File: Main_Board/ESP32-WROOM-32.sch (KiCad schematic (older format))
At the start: 19 parts, among them J1 USB_B_Micro, Q1 mmbt2222, Q2 mmbt2222, U1 CP2104, U3 ESP32-WROOM-32

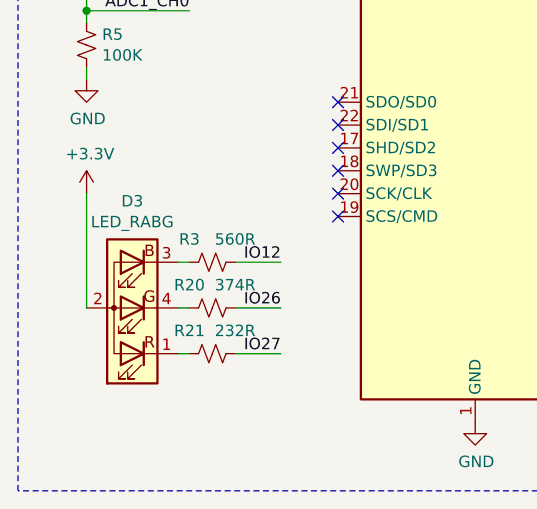
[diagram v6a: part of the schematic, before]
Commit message: New D3 footprint and model
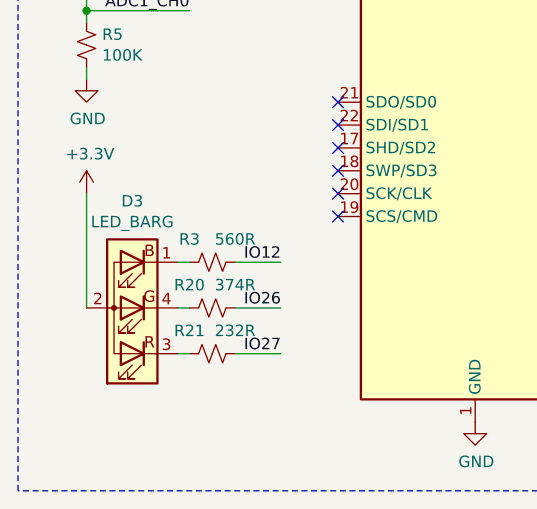
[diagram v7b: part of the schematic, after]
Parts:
- removed D3: LED_RABG, Main_Board:LED_QBLP655R_RGB, symbol Device:LED_RABG
- added D3: LED_BARG, Main_Board:LED-160-80180, symbol Device:LED_BARG
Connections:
- net +3V3: now also D3.2 (A)
- net at R3.2: now also D3.1 (BK)
- net at R20.2: now also D3.4 (GK)
- net at R21.2: now also D3.3 (RK)
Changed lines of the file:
@@
 	3400 3650 3650 3650
 NoConn ~ 3400 2450
+NoConn ~ 2200 2950
+NoConn ~ 2200 3050
 $Comp
-L Device:LED_RABG D3
-U 1 1 5FFE32BD
+L Device:LED_BARG D3
+U 1 1 60BEE694
 P 1300 3850
 F 0 "D3" H 1300 3383 50  0000 C CNN
-F 1 "LED_RABG" H 1300 3474 50  0000 C CNN
-F 2 "Main_Board:LED_QBLP655R_RGB" H 1300 3800 50  0001 C CNN
-F 3 "https://static6.arrow.com/aropdfconversion/2e9f9b5de02200d8efd894b12d78141ca956a5cd/qblp655-rgb.pdf" H 1300 3800 50  0001 C CNN
-F 4 "QBLP655-RGB" H 1300 3850 50  0001 C CNN "*Arrow"
+F 1 "LED_BARG" H 1300 3474 50  0000 C CNN
+F 2 "Main_Board:LED-160-80180" H 1300 3800 50  0001 C CNN
+F 3 "https://www.sycelectronica.com.ar/optoelectronica/LED-160-80180.pdf" H 1300 3800 50  0001 C CNN
 	1    1300 3850
 	-1   0    0    1
 $EndComp
-NoConn ~ 2200 2950
-NoConn ~ 2200 3050
 $EndSCHEMATC

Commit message: C2, C3, C8 and C14 footprints and packages changed from 1210 to 0603 (#11)
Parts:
- C14: footprint Capacitor_SMD:C_1210_3225Metric_Pad1.42x2.65mm_HandSolder -> Capacitor_SMD:C_0603_1608Metric_Pad1.08x0.95mm_HandSolder
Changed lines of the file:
@@
 F 0 "C14" H 5242 1646 50  0000 L CNN
 F 1 "10uF 6.3V X5R" H 5242 1555 50  0000 L CNN
-F 2 "Capacitor_SMD:C_1210_3225Metric_Pad1.42x2.65mm_HandSolder" H 5150 1600 50  0001 C CNN
+F 2 "Capacitor_SMD:C_0603_1608Metric_Pad1.08x0.95mm_HandSolder" H 5150 1600 50  0001 C CNN
 F 3 "https://static6.arrow.com/aropdfconversion/f7a2596b5312288600ca127f041a86c0cac4c78c/grm188r60j106ke47.pdf" H 5150 1600 50  0001 C CNN
 F 4 "12103C106KAT2A" H 5150 1600 50  0001 C CNN "*Digikey"
